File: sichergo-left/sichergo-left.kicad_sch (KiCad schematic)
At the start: 35 parts, among them J1 Conn_01x04_Pin, Q2 2N7002, U1 AZ1117-3.3, U2 TPD4E05U06DQA, U3 YTS1C0033BBG01, U4 STM32F103C8Tx, U5 SN74LVC1G125DBV, U6 SN74LVC1G125DBV, Y1 Crystal_GND24

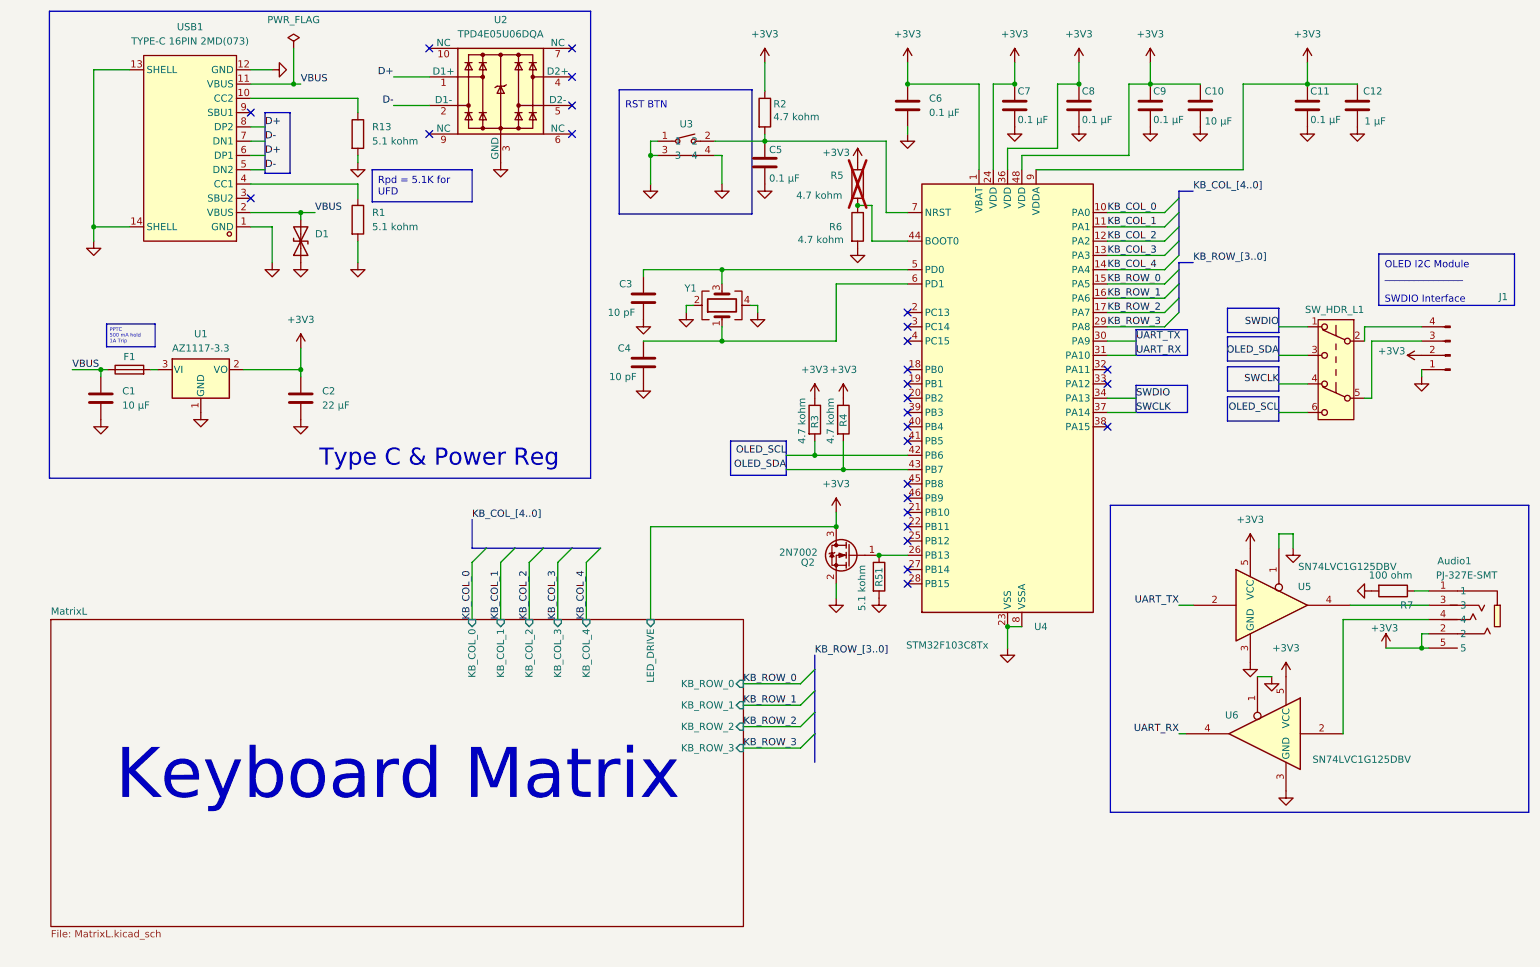
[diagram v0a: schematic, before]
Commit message: Split design in two PCBs and remake layout
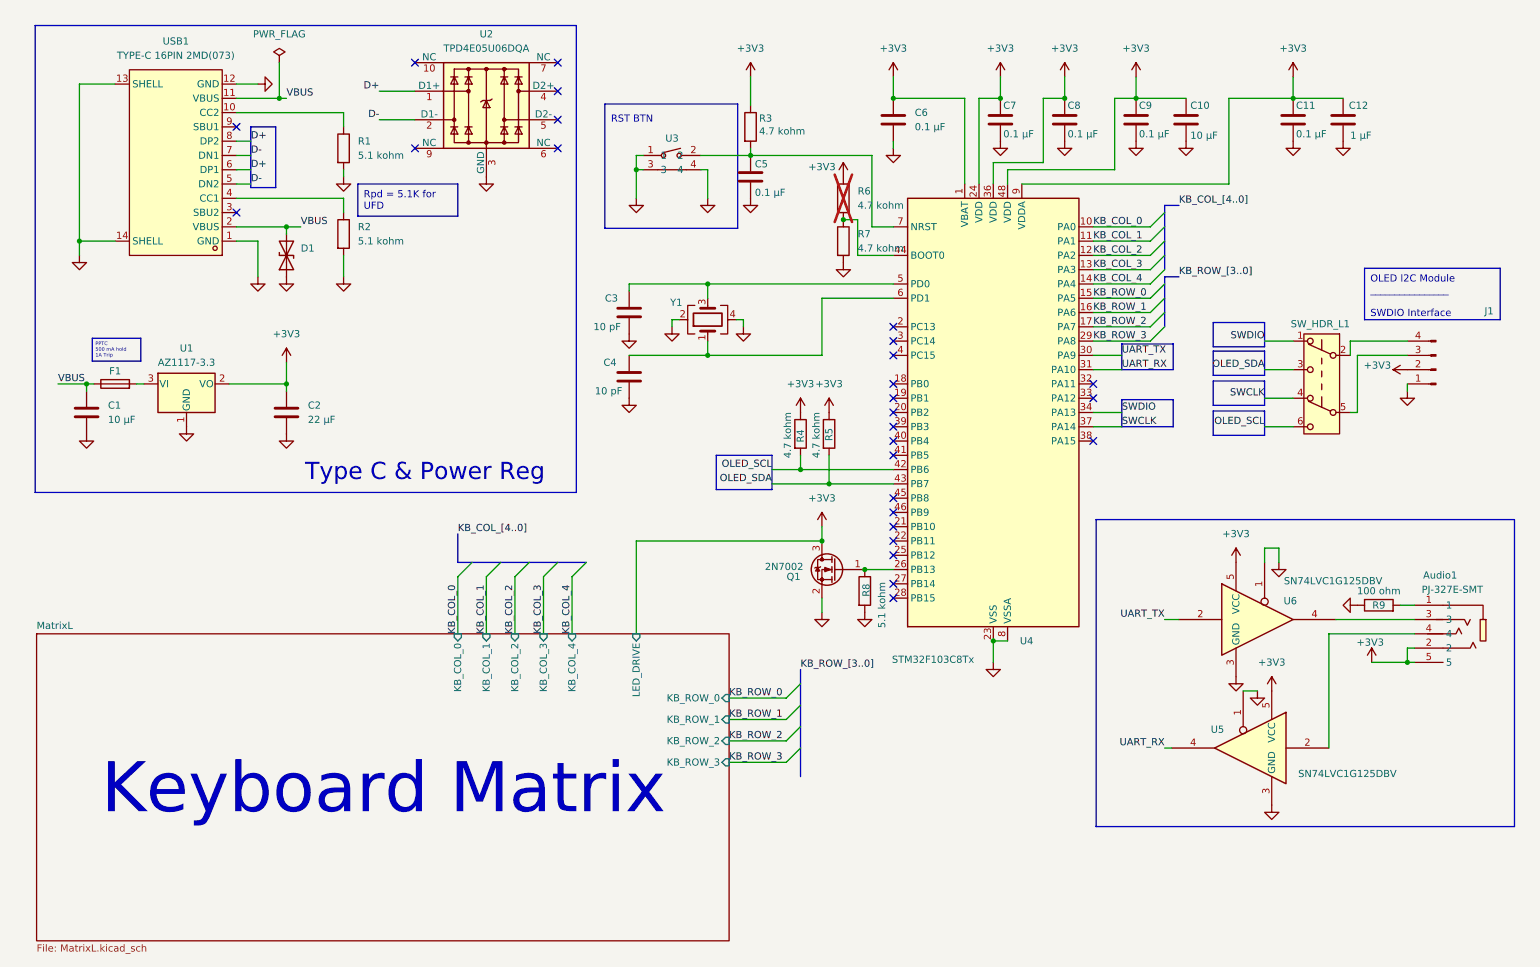
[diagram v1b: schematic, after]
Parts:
- removed Q2: 2N7002, Package_TO_SOT_SMD:SOT-23_Handsoldering, symbol Transistor_FET:2N7002
- removed R13: 5.1 kohm, Resistor_SMD:R_0603_1608Metric_Pad0.98x0.95mm_HandSolder, symbol #inventree:RC0603FR-075K1L
- removed R2: 4.7 kohm, Resistor_SMD:R_0603_1608Metric_Pad0.98x0.95mm_HandSolder, symbol #inventree:RC0603FR-074K7L
- removed R5, R6: 4.7 kohm, symbol #inventree:ERJ-6GEYJ472V
- removed R51: 5.1 kohm, Resistor_SMD:R_0612_1632Metric_Pad1.18x3.40mm_HandSolder, symbol #inventree:RC0603FR-075K1L
- removed R7: 100 ohm, Resistor_SMD:R_0805_2012Metric_Pad1.20x1.40mm_HandSolder, symbol #inventree:ERJ-6GEYJ101V
- added Q1: 2N7002, Package_TO_SOT_SMD:SOT-23_Handsoldering, symbol Transistor_FET:2N7002
- added R2, R8: 5.1 kohm, Resistor_SMD:R_0603_1608Metric_Pad0.98x0.95mm_HandSolder, symbol #inventree:RC0603FR-075K1L
- added R5: 4.7 kohm, symbol #inventree:RC0603FR-074K7L
- added R6, R7: 4.7 kohm, Resistor_SMD:R_0603_1608Metric_Pad0.98x0.95mm_HandSolder, symbol #inventree:RC0603FR-074K7L
- added R9: 100 ohm, Resistor_SMD:R_0603_1608Metric_Pad0.98x0.95mm_HandSolder, symbol #inventree:RC0603FR-07100RL
- R3: footprint (none) -> Resistor_SMD:R_0603_1608Metric_Pad0.98x0.95mm_HandSolder
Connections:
- net +3V3: now also Q1.3 (D), R5.1, R6.1
- net GND: now also Q1.2 (S), R2.2, R7.2, R8.2, R9.1
- net OLED_SCL: now also R4.2; no longer R3.2
- net OLED_SDA: now also R5.2; no longer R4.2
- net UART_RX: now also U5.4; no longer U6.4
- net UART_TX: now also U6.2; no longer U5.2
- net at USB1.10 (CC2): now also R1.1
- net at USB1.4 (CC1): now also R2.1; no longer R1.1
- net at U4.26 (PB13): now also Q1.1 (G), R8.1
- net at U4.44 (BOOT0): now also R6.2, R7.1
- net at C5.1, U3.2, U4.7 (NRST): now also R3.2
- net at Audio1.4: now also U5.2; no longer U6.2
- net at Audio1.1: now also R9.2
- net at Audio1.3: now also U6.4; no longer U5.4

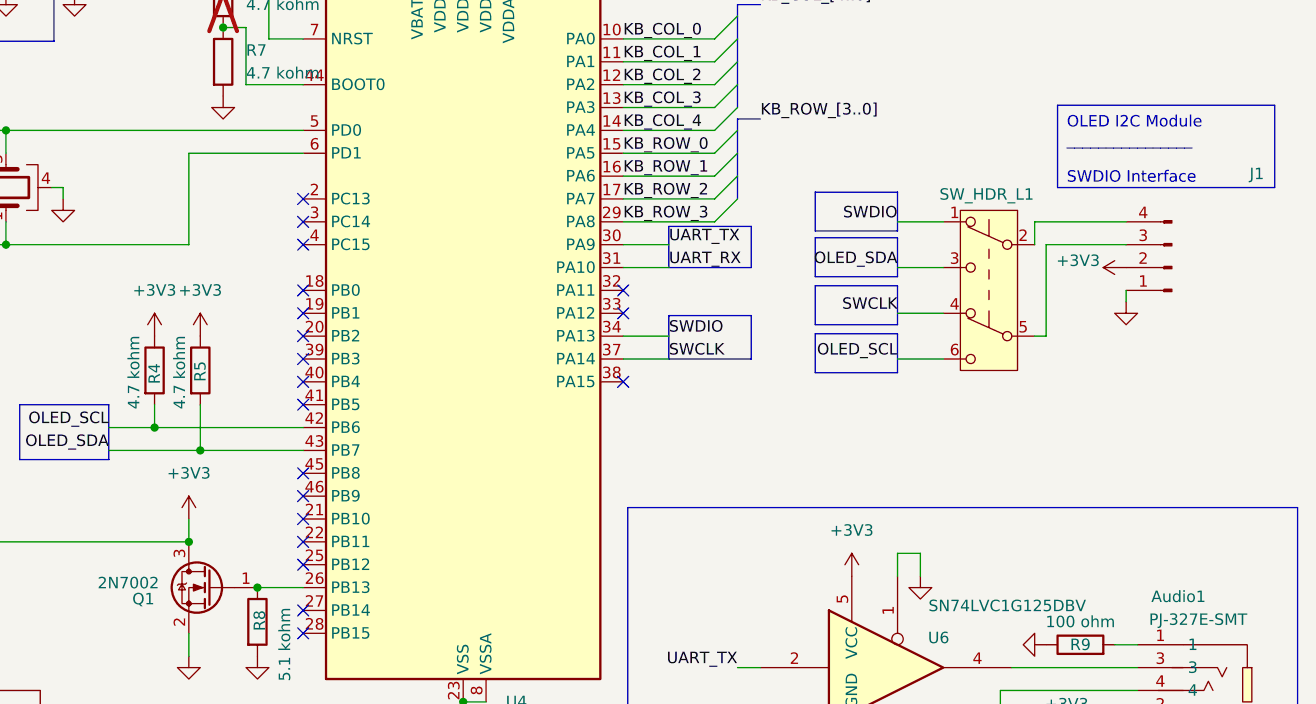
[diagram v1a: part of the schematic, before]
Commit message: Route left side
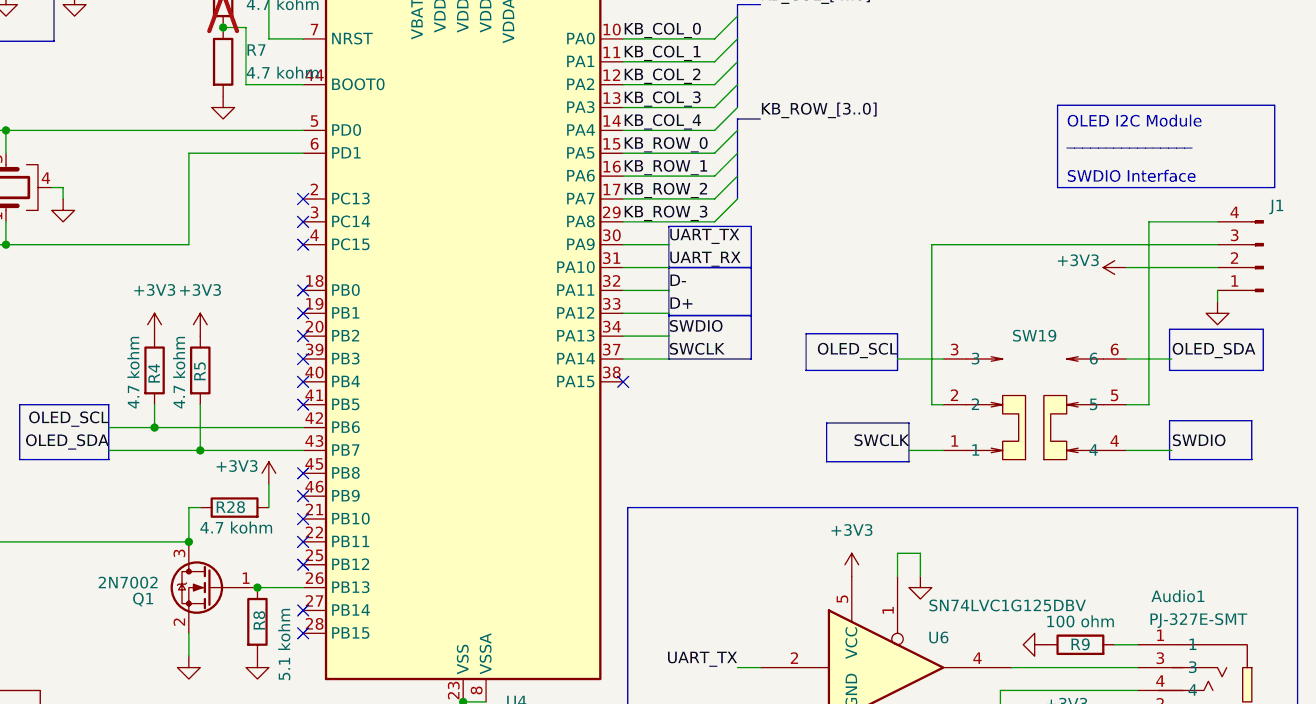
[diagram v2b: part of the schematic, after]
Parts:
- removed SW_HDR_L1: SW_Push_DPDT, symbol Switch:SW_Push_DPDT
- added R28: 4.7 kohm, Resistor_SMD:R_0603_1608Metric_Pad0.98x0.95mm_HandSolder, symbol #inventree:RC0603FR-074K7L
- added SW19: MS-22C01-G010, easyeda2kicad:SW-SMD_6P-L7.2-W3.5-P2.50-LS6.0-TL, symbol easyeda2kicad:MS-22C01-G010
- C1, C10, C11, C12, C2, C3, C4, C5, C6, C7, C8, C9: footprint 0805 (2012 Metric) -> Capacitor_SMD:C_0805_2012Metric_Pad1.18x1.45mm_HandSolder
- R4, R5: footprint (none) -> Resistor_SMD:R_0603_1608Metric_Pad0.98x0.95mm_HandSolder
- U4: InvenTree (none) -> 55
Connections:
- net +3V3: now also R28.2; no longer Q1.3 (D)
- net D+: now also U4.33 (PA12)
- net D-: now also U4.32 (PA11)
- net OLED_SCL: now also SW19.3
- net OLED_SDA: now also SW19.6
- net SWCLK: now also SW19.1
- net SWDIO: now also SW19.4
- net at J1.3 (Pin_3): now also SW19.2
- net at J1.4 (Pin_4): now also SW19.5
- new net MatrixL/LED_DRIVE: Q1.3 (D), R28.1
- no-connect marks 27 -> 25
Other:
- moved on the sheet: J1

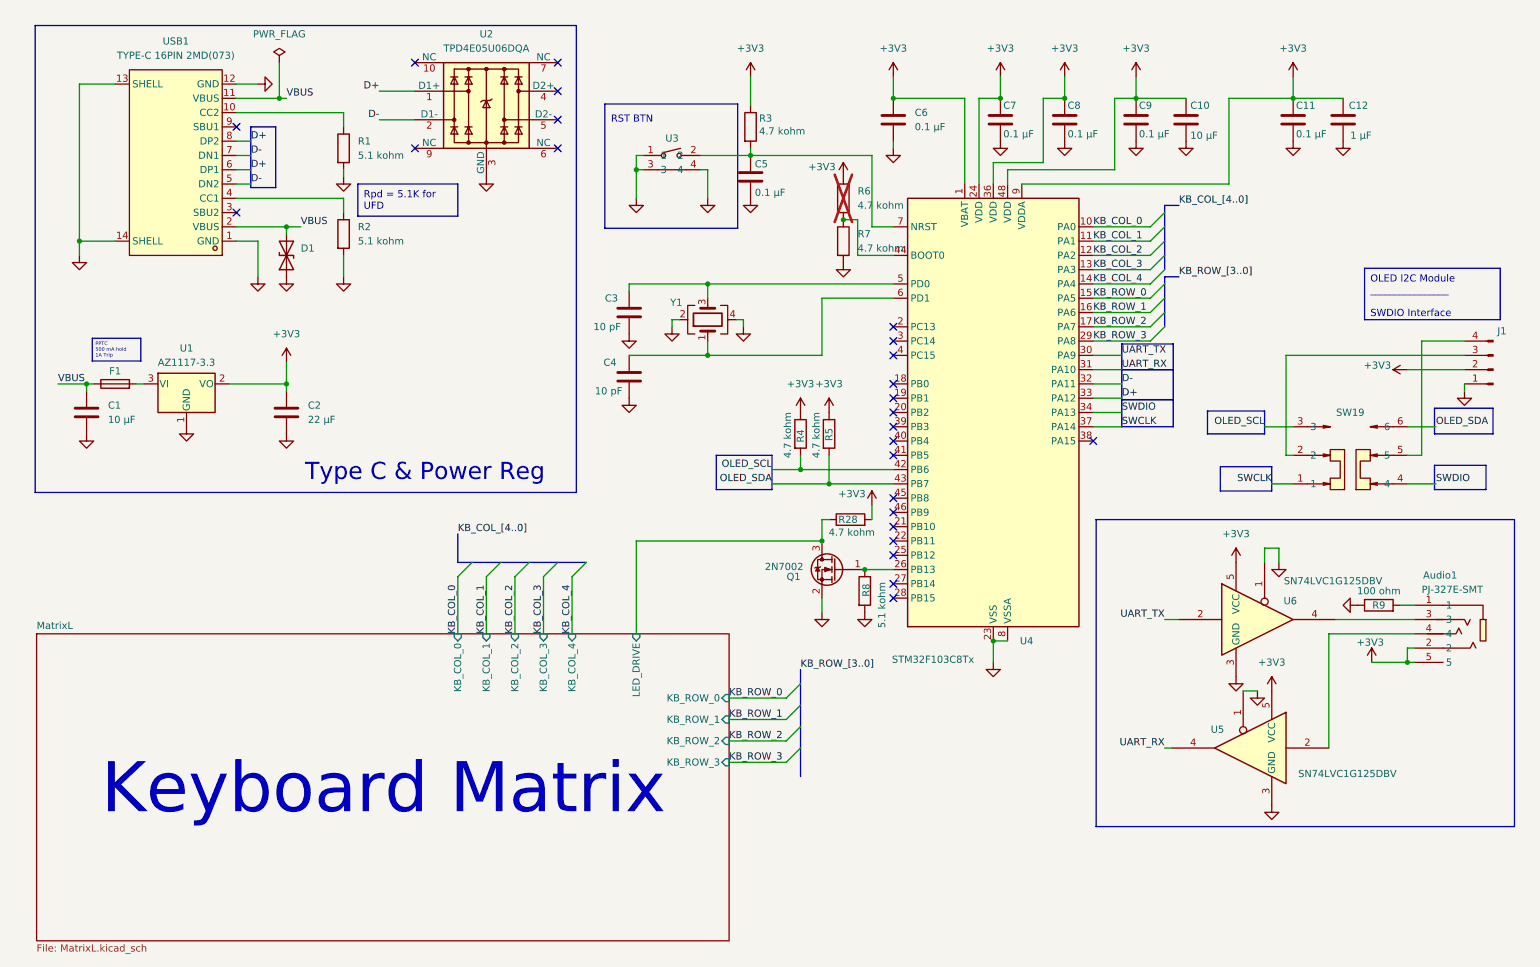
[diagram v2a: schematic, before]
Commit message: Reroute everything
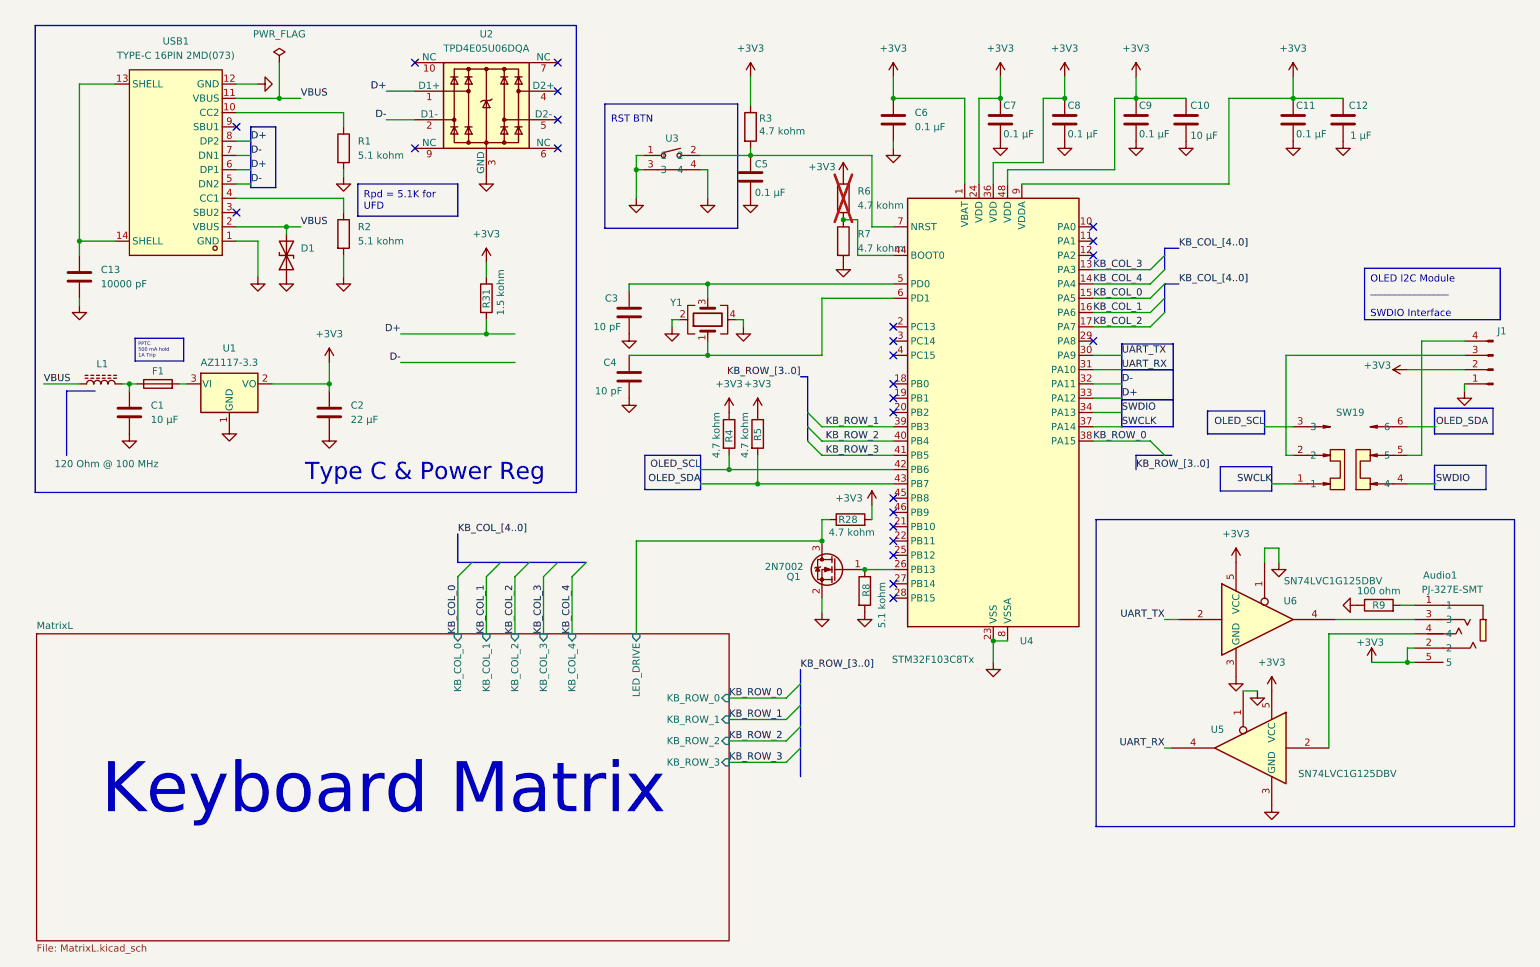
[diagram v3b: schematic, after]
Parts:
- added C13: 10000 pF, Capacitor_SMD:C_0805_2012Metric_Pad1.18x1.45mm_HandSolder, symbol #inventree:CL21B103KBANNNC
- added L1: 120 Ohm @ 100 MHz, Inductor_SMD:L_0603_1608Metric_Pad1.05x0.95mm_HandSolder, symbol Device:L_Ferrite
- added R31: 1.5 kohm, Resistor_SMD:R_0603_1608Metric_Pad0.98x0.95mm_HandSolder, symbol #inventree:RC0603FR-071K5L
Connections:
- net +3V3: now also R31.1
- net D+: now also R31.2
- net GND: now also C13.2; no longer USB1.13 (SHELL), USB1.14 (SHELL)
- net KB_COL_0: now also U4.15 (PA5); no longer U4.10 (PA0)
- net KB_COL_1: now also U4.16 (PA6); no longer U4.11 (PA1)
- net KB_COL_2: now also U4.17 (PA7); no longer U4.12 (PA2)
- net KB_ROW_0: now also U4.38 (PA15); no longer U4.15 (PA5)
- net KB_ROW_1: now also U4.39 (PB3); no longer U4.16 (PA6)
- net KB_ROW_2: now also U4.40 (PB4); no longer U4.17 (PA7)
- net KB_ROW_3: now also U4.41 (PB5); no longer U4.29 (PA8)
- net VBUS: now also L1.1; no longer C1.1, F1.1
- new net: C1.1, F1.1, L1.2
- new net: C13.1, USB1.13 (SHELL), USB1.14 (SHELL)
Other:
- moved on the sheet: C1, C2, F1, R4, R5, U1
